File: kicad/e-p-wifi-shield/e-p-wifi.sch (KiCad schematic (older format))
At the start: 38 parts, among them J1 Shunt, J2 Vbat1, J3 Masse T1, J4 Température, J5 Vbat2, J6 Conn_02x14_MKR1010, SW1 StSp - Farnell 986-501, SW2 Sleep - Farnell 986-501, SW3 Conrad 711771, SW4 BP APEM - Farnell 108-2512

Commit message: Modification du shield MKR wifi 1010
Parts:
- SW4: symbol Switch:SW_Push -> e-p-wifi-rescue:SW_Push
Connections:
- net GND: now also SW4.3, SW4.4
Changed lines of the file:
@@
 	4850 5250 4850 3500
 $Comp
-L Switch:SW_Push SW4
+L e-p-wifi-rescue:SW_Push SW4
 U 1 1 5DD68AC4
 P 3350 6450
-F 0 "SW4" H 3350 6300 50  0000 C CNN
+F 0 "SW4" H 3351 6360 50  0000 C CNN
 F 1 "BP APEM - Farnell 108-2512" H 3500 6600 50  0000 C CNN
 F 2 "e-p-wifi-v2:BP" H 3350 6650 50  0001 C CNN
@@
 P 3100 6450
 F 0 "#PWR011" H 3100 6300 50  0001 C CNN
-F 1 "+3.3V" V 3088 6563 50  0000 L CNN
+F 1 "+3.3V" V 3178 6443 50  0000 L CNN
 F 2 "" H 3100 6450 50  0001 C CNN
 F 3 "" H 3100 6450 50  0001 C CNN
@@
 Text Notes 3700 6450 0    50   ~ 10
 meross
-Wire Notes Line
-	3600 6200 3600 6700
-Wire Notes Line
-	3600 6700 3200 6700
-Wire Notes Line
-	3200 6700 3200 6200
-Wire Notes Line
-	3200 6200 3150 6200
 Wire Wire Line
 	4800 1670 4800 3400
@@
 Wire Notes Line
 	2850 7150 2850 6350
+$Comp
+L power:GND #PWR0101
+U 1 1 5E995A20
+P 3552 6701
+F 0 "#PWR0101" H 3552 6451 50  0001 C CNN
+F 1 "GND" H 3557 6528 50  0000 C CNN
+F 2 "" H 3552 6701 50  0001 C CNN
+F 3 "" H 3552 6701 50  0001 C CNN
+	1    3552 6701
+	1    0    0    -1
+$EndComp
+Wire Wire Line
+	3550 6600 3550 6692
+Wire Wire Line
+	3550 6694 3552 6694
+Wire Wire Line
+	3552 6694 3552 6701
+Wire Wire Line
+	3150 6600 3150 6692
+Wire Wire Line
+	3150 6692 3550 6692
+Connection ~ 3550 6692
+Wire Wire Line
+	3550 6692 3550 6694
+Wire Notes Line
+	3624 6188 3624 6662
+Wire Notes Line
+	3624 6662 3142 6662
+Wire Notes Line
+	3142 6662 3142 6187
 $EndSCHEMATC

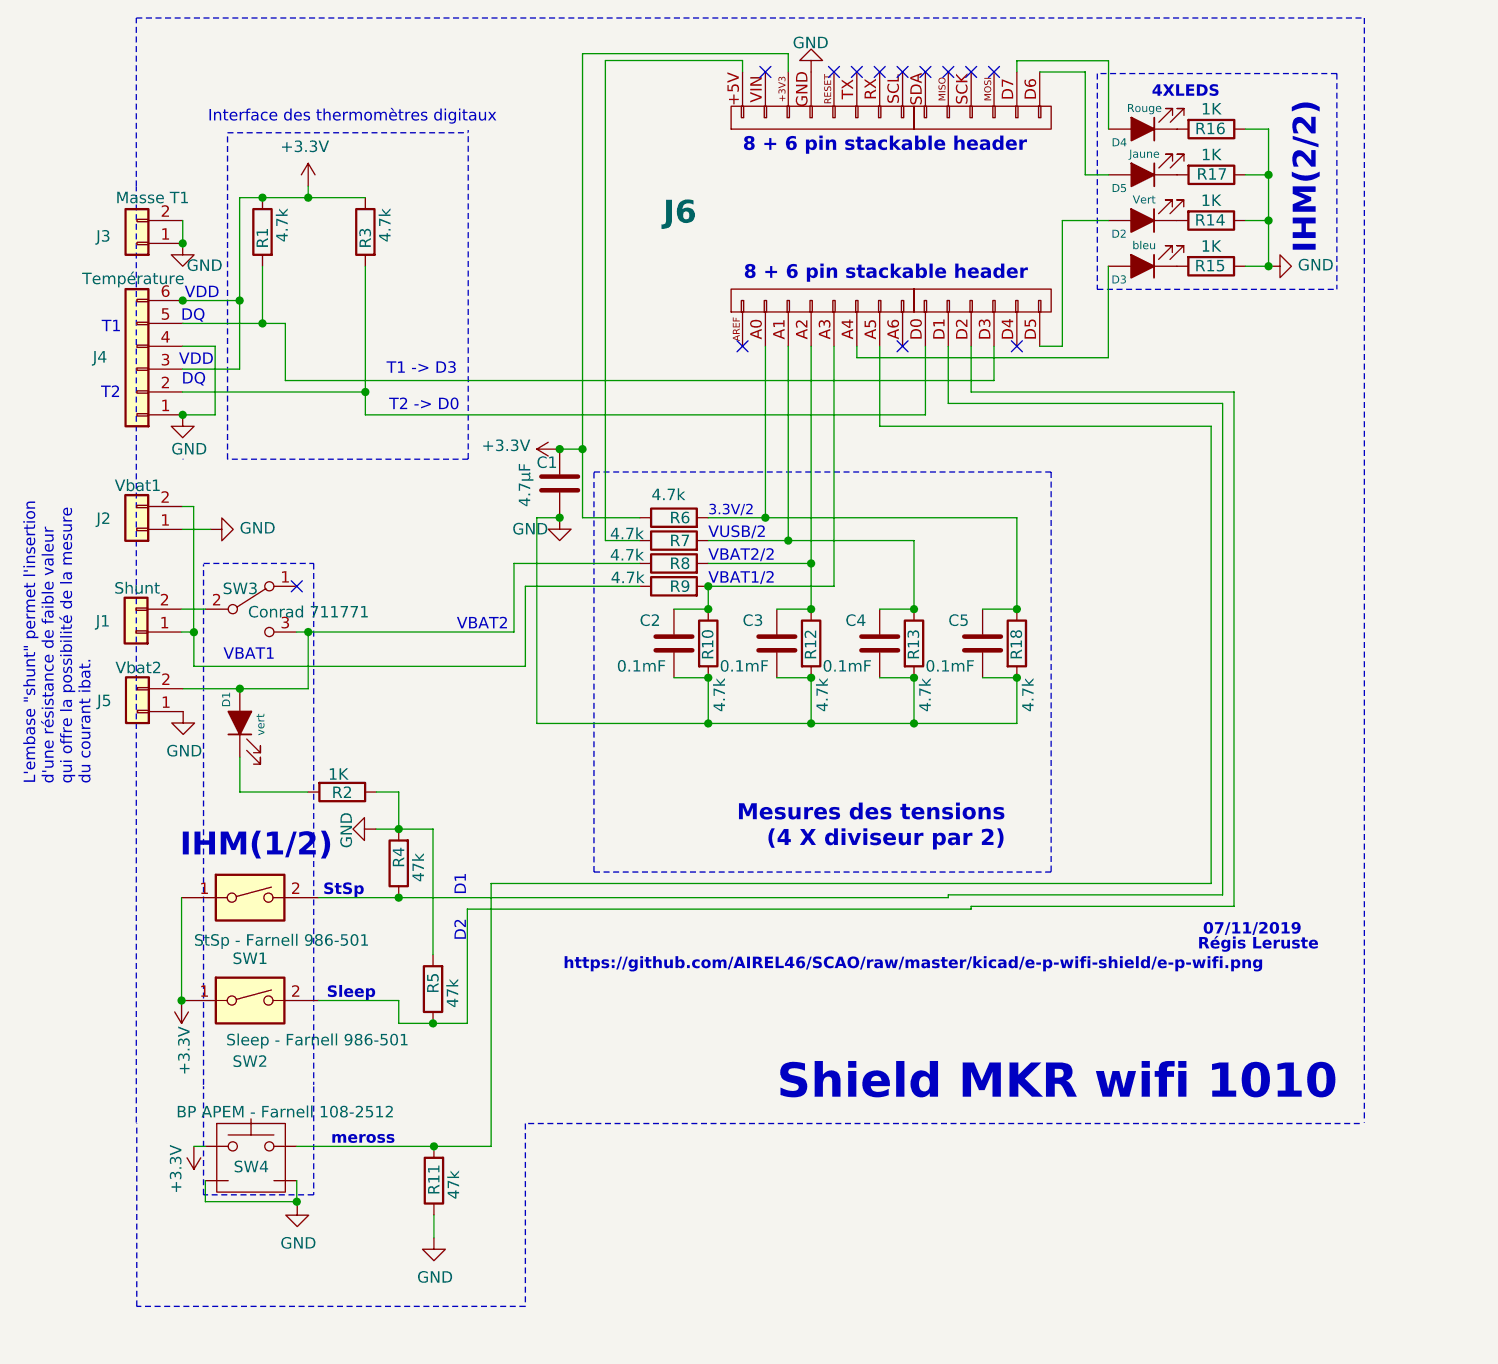
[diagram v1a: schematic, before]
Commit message: Modification du shield MKR wifi 1010
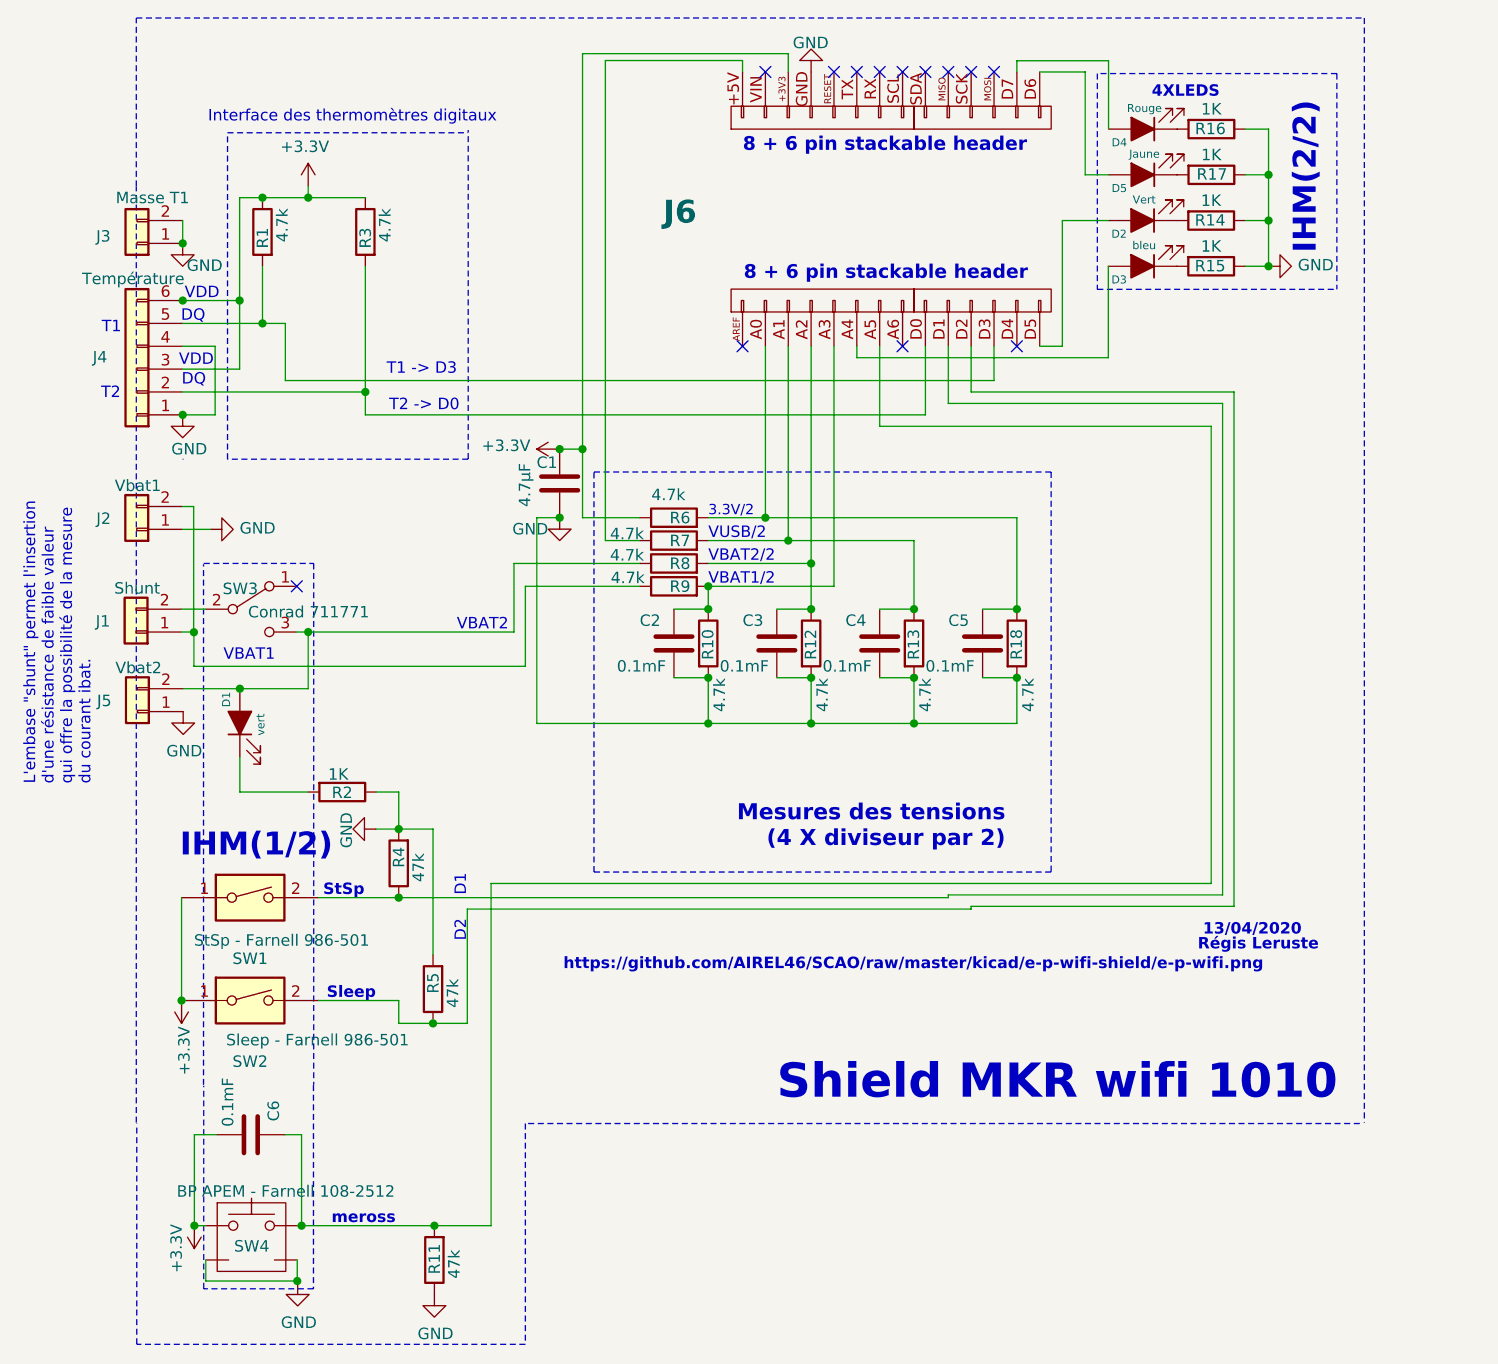
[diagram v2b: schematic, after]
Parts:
- added C6: 0.1mF, Capacitor_THT:C_Disc_D3.0mm_W1.6mm_P2.50mm, symbol Device:C
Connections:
- net +3V3: now also C6.2
- net at J6.A5 (Pin_7), R11.2, SW4.2: now also C6.1
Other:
- note added: "13/04/2020"
- note removed: "07/11/2019"
- moved on the sheet: R11, SW4
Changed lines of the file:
@@
 Sheet 1 1
 Title "Shield du MKR wifi 1010"
-Date "2019-11-03"
-Rev "1.0"
-Comp "Quiet cook"
+Date "2020-04-13"
+Rev "1.1"
+Comp "A3C Presqu'île"
 Comment1 ""
 Comment2 ""
@@
 $EndBitmap
 Text Notes 7514 5535 0    50   ~ 10
-07/11/2019
+13/04/2020
 Text Notes 7491 5600 0    50   ~ 10
 Régis Leruste
@@
 L e-p-wifi-rescue:SW_Push SW4
 U 1 1 5DD68AC4
-P 3350 6450
-F 0 "SW4" H 3351 6360 50  0000 C CNN
-F 1 "BP APEM - Farnell 108-2512" H 3500 6600 50  0000 C CNN
-F 2 "e-p-wifi-v2:BP" H 3350 6650 50  0001 C CNN
-F 3 "http://www.farnell.com/datasheets/10672.pdf?_ga=1.98306207.1823820493.1466675868" H 3350 6650 50  0001 C CNN
-	1    3350 6450
+P 3352 6797
+F 0 "SW4" H 3353 6707 50  0000 C CNN
+F 1 "BP APEM - Farnell 108-2512" H 3502 6947 50  0000 C CNN
+F 2 "e-p-wifi-v2:BP" H 3352 6997 50  0001 C CNN
+F 3 "http://www.farnell.com/datasheets/10672.pdf?_ga=1.98306207.1823820493.1466675868" H 3352 6997 50  0001 C CNN
+	1    3352 6797
 	1    0    0    -1
 $EndComp
@@
 L power:+3.3V #PWR011
 U 1 1 5DD6A987
-P 3100 6450
-F 0 "#PWR011" H 3100 6300 50  0001 C CNN
-F 1 "+3.3V" V 3178 6443 50  0000 L CNN
-F 2 "" H 3100 6450 50  0001 C CNN
-F 3 "" H 3100 6450 50  0001 C CNN
-	1    3100 6450
-	-1   0    0    1
-$EndComp
-Wire Wire Line
-	3100 6450 3150 6450
+P 3102 6797
+F 0 "#PWR011" H 3102 6647 50  0001 C CNN
+F 1 "+3.3V" V 3180 6790 50  0000 L CNN
+F 2 "" H 3102 6797 50  0001 C CNN
+F 3 "" H 3102 6797 50  0001 C CNN
+	1    3102 6797
+	-1   0    0    1
+$EndComp
+Wire Wire Line
+	3102 6797 3152 6797
 $Comp
 L Device:R R11
 U 1 1 5DD7205E
-P 4150 6600
-F 0 "R11" V 4149 6528 50  0000 L CNN
-F 1 "47k" V 4063 6555 50  0000 L CNN
-F 2 "Resistor_THT:R_Axial_DIN0207_L6.3mm_D2.5mm_P7.62mm_Horizontal" V 4080 6600 50  0001 C CNN
-F 3 "~" H 4150 6600 50  0001 C CNN
-	1    4150 6600
+P 4152 6947
+F 0 "R11" V 4151 6875 50  0000 L CNN
+F 1 "47k" V 4065 6902 50  0000 L CNN
+F 2 "Resistor_THT:R_Axial_DIN0207_L6.3mm_D2.5mm_P7.62mm_Horizontal" V 4082 6947 50  0001 C CNN
+F 3 "~" H 4152 6947 50  0001 C CNN
+	1    4152 6947
 	-1   0    0    1
 $EndComp
@@
 L power:GND #PWR013
 U 1 1 5DD74324
-P 4150 6850
-F 0 "#PWR013" H 4150 6600 50  0001 C CNN
-F 1 "GND" H 4155 6677 50  0000 C CNN
-F 2 "" H 4150 6850 50  0001 C CNN
-F 3 "" H 4150 6850 50  0001 C CNN
-	1    4150 6850
-	1    0    0    -1
-$EndComp
-Wire Wire Line
-	3550 6450 4150 6450
+P 4152 7097
+F 0 "#PWR013" H 4152 6847 50  0001 C CNN
+F 1 "GND" H 4157 6924 50  0000 C CNN
+F 2 "" H 4152 7097 50  0001 C CNN
+F 3 "" H 4152 7097 50  0001 C CNN
+	1    4152 7097
+	1    0    0    -1
+$EndComp
 Wire Wire Line
 	6100 2950 6100 3300
@@
 Wire Wire Line
 	7550 5300 4400 5300
-Wire Wire Line
-	4400 5300 4400 6450
-Wire Wire Line
-	4400 6450 4150 6450
-Connection ~ 4150 6450
-Text Notes 3700 6450 0    50   ~ 10
+Text Notes 3702 6797 0    50   ~ 10
 meross
 Wire Wire Line
@@
 	5800 4600 6250 4600
 Wire Wire Line
-	4150 6750 4150 6850
-Wire Wire Line
 	5350 4600 4600 4600
 Wire Wire Line
@@
 	8200 6350 4550 6350
 Wire Notes Line
-	4550 6350 4550 7150
-Wire Notes Line
-	4550 7150 2850 7150
-Wire Notes Line
 	2850 7150 2850 6350
+Wire Wire Line
+	3552 7041 3554 7041
+Wire Wire Line
+	3554 7041 3554 7048
+Wire Wire Line
+	3152 6947 3152 7039
+Wire Wire Line
+	3152 7039 3552 7039
+Wire Wire Line
+	3552 7039 3552 7041
+Wire Wire Line
+	3552 6947 3552 7039
+Connection ~ 3552 7039
 $Comp
 L power:GND #PWR0101
 U 1 1 5E995A20
-P 3552 6701
-F 0 "#PWR0101" H 3552 6451 50  0001 C CNN
-F 1 "GND" H 3557 6528 50  0000 C CNN
-F 2 "" H 3552 6701 50  0001 C CNN
-F 3 "" H 3552 6701 50  0001 C CNN
-	1    3552 6701
-	1    0    0    -1
-$EndComp
-Wire Wire Line
-	3550 6600 3550 6692
-Wire Wire Line
-	3550 6694 3552 6694
-Wire Wire Line
-	3552 6694 3552 6701
-Wire Wire Line
-	3150 6600 3150 6692
-Wire Wire Line
-	3150 6692 3550 6692
-Connection ~ 3550 6692
-Wire Wire Line
-	3550 6692 3550 6694
-Wire Notes Line
-	3624 6188 3624 6662
-Wire Notes Line
-	3624 6662 3142 6662
-Wire Notes Line
-	3142 6662 3142 6187
+P 3554 7048
+F 0 "#PWR0101" H 3554 6798 50  0001 C CNN
+F 1 "GND" H 3559 6875 50  0000 C CNN
+F 2 "" H 3554 7048 50  0001 C CNN
+F 3 "" H 3554 7048 50  0001 C CNN
+	1    3554 7048
+	1    0    0    -1
+$EndComp
+$Comp
+L Device:C C6
+U 1 1 5E9942DE
+P 3349 6399
+F 0 "C6" H 3199 6499 50  0000 L CNN
+F 1 "0.1mF" H 3099 6299 50  0000 L CNN
+F 2 "Capacitor_THT:C_Disc_D3.0mm_W1.6mm_P2.50mm" H 3387 6249 50  0001 C CNN
+F 3 "~" H 3349 6399 50  0001 C CNN
+	1    3349 6399
+	0    1    1    0
+$EndComp
+Wire Wire Line
+	3552 6797 3571 6797
+Wire Wire Line
+	3499 6399 3571 6399
+Wire Wire Line
+	3571 6399 3571 6797
+Connection ~ 3571 6797
+Wire Wire Line
+	3571 6797 4152 6797
+Wire Wire Line
+	3102 6798 3102 6797
+Wire Wire Line
+	3102 6399 3199 6399
+Connection ~ 3102 6797
+Wire Wire Line
+	3102 6797 3102 6399
+Wire Wire Line
+	4400 5300 4400 6797
+Wire Wire Line
+	4400 6797 4152 6797
+Connection ~ 4152 6797
+Wire Notes Line
+	3623 6182 3623 7073
+Wire Notes Line
+	3623 7073 3143 7073
+Wire Notes Line
+	3143 7073 3143 6185
+Wire Notes Line
+	4550 7316 2850 7316
+Wire Notes Line
+	2850 7316 2850 7155
+Wire Notes Line
+	4550 6350 4550 7316
 $EndSCHEMATC

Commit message: mise à jour kicad
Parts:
- J4: footprint Connector_PinHeader_2.54mm:PinHeader_1x06_P2.54mm_Vertical -> e-p-wifi-v2:PinHeader_1x06_P2.54mm_Vertical_J4
- J6: footprint e-p-wifi-v2:PinSocket_2x14_MKR1010 -> e-p-wifi-v2:PinSocket_2x14_MKR1010_ov
- SW1: footprint e-p-wifi-v2:jumper-switch -> e-p-wifi-v2:jumper-switch-sw1
- SW2: footprint e-p-wifi-v2:jumper-switch -> e-p-wifi-v2:jumper-switch-sw2
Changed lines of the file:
@@
 F 0 "SW1" H 3346 5095 50  0000 C CNN
 F 1 "StSp - Farnell 986-501" H 3484 5175 50  0000 C CNN
-F 2 "e-p-wifi-v2:jumper-switch" H 3346 5362 50  0001 C CNN
+F 2 "e-p-wifi-v2:jumper-switch-sw1" H 3346 5362 50  0001 C CNN
 F 3 "http://www.farnell.com/datasheets/58539.pdf?_ga=2.27608380.140208918.1573048803-1966718086.1557591461&_gac=1.121467258.1573048803.Cj0KCQiA-4nuBRCnARIsAHwyuPqR51EVzwLC_rjGxuRlpl_aeelUyUlwni0GneFg4tO4wrwk64y3RFoaAuRiEALw_wcB" H 3346 5362 50  0001 C CNN
 	1    3346 5362
@@
 F 0 "SW2" H 3346 5545 50  0000 C CNN
 F 1 "Sleep - Farnell 986-501" H 3641 5639 50  0000 C CNN
-F 2 "e-p-wifi-v2:jumper-switch" H 3346 5812 50  0001 C CNN
+F 2 "e-p-wifi-v2:jumper-switch-sw2" H 3346 5812 50  0001 C CNN
 F 3 "http://www.farnell.com/datasheets/58539.pdf?_ga=2.27608380.140208918.1573048803-1966718086.1557591461&_gac=1.121467258.1573048803.Cj0KCQiA-4nuBRCnARIsAHwyuPqR51EVzwLC_rjGxuRlpl_aeelUyUlwni0GneFg4tO4wrwk64y3RFoaAuRiEALw_wcB" H 3346 5812 50  0001 C CNN
 	1    3346 5812
@@
 F 0 "J6" V 6487 3697 100 0000 R CNB
 F 1 "Conn_02x14_MKR1010" V 6479 3339 75  0001 R CNB
-F 2 "e-p-wifi-v2:PinSocket_2x14_MKR1010" V 6249 2680 50  0001 C CNN
+F 2 "e-p-wifi-v2:PinSocket_2x14_MKR1010_ov" V 6249 2680 50  0001 C CNN
 F 3 "~" H 6100 2750 50  0001 C CNN
 	1    6100 2750
@@
 F 0 "J4" H 3013 2998 50  0000 C CNN
 F 1 "Température" H 2867 2655 50  0000 C CNN
-F 2 "Connector_PinHeader_2.54mm:PinHeader_1x06_P2.54mm_Vertical" H 2851 3050 50  0001 C CNN
+F 2 "e-p-wifi-v2:PinHeader_1x06_P2.54mm_Vertical_J4" H 2851 3050 50  0001 C CNN
 F 3 "~" H 2851 3050 50  0001 C CNN
 	1    2851 3050
@@
 Wire Notes Line
 	2848 6346 2848 2252
-Text Notes 5650 6261 0    150  ~ 30
-Shield MKR wifi 1010
 $Comp
 L Connector_Generic:Conn_01x02 J2
@@
 Connection ~ 5800 4100
 Wire Wire Line
-	5350 3800 5700 3800
-Wire Wire Line
 	6250 3800 6250 4100
 Connection ~ 6250 4100
-Wire Wire Line
-	5600 3700 6700 3700
 Wire Wire Line
 	6700 3700 6700 4100
 Connection ~ 5600 3700
 Connection ~ 6700 4100
-Wire Wire Line
-	5700 2950 5700 3800
-Connection ~ 5700 3800
-Wire Wire Line
-	5700 3800 6250 3800
 Wire Wire Line
 	5800 2950 5800 3900
@@
 Wire Notes Line
 	4550 6350 4550 7316
+Wire Wire Line
+	5350 3800 5700 3800
+Wire Wire Line
+	5600 3700 6700 3700
+Connection ~ 5700 3800
+Wire Wire Line
+	5700 3800 6250 3800
+Text Notes 5650 6261 0    150  ~ 30
+Shield MKR wifi 1010
+Wire Wire Line
+	5700 2950 5700 3800
 $EndSCHEMATC
